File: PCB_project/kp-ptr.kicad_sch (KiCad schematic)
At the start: 41 parts, among them J1 ESP32_PROG_CON, J3 Conn_02x02_Odd_Even, U1 ESP32-S3FN8, Y1 7M40000005-40MHz

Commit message: Schematic updated
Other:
- title: KP-PTR -> KP-PTR project - PTR_mini
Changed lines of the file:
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@@
 	(paper "A4")
 	(title_block
-		(title "KP-PTR")
-		(date "2023-12-10")
-		(rev "1.1")
+		(title "KP-PTR project - PTR_mini")
+		(date "2026-09-17")
+		(rev "1.0")
 		(company "Polskie Towarzystwo Rakietowe")
 		(comment 1 "bartekM, FlyingBanana, Kretu, Red Labs, Stachu M, U.S. air force i inni")

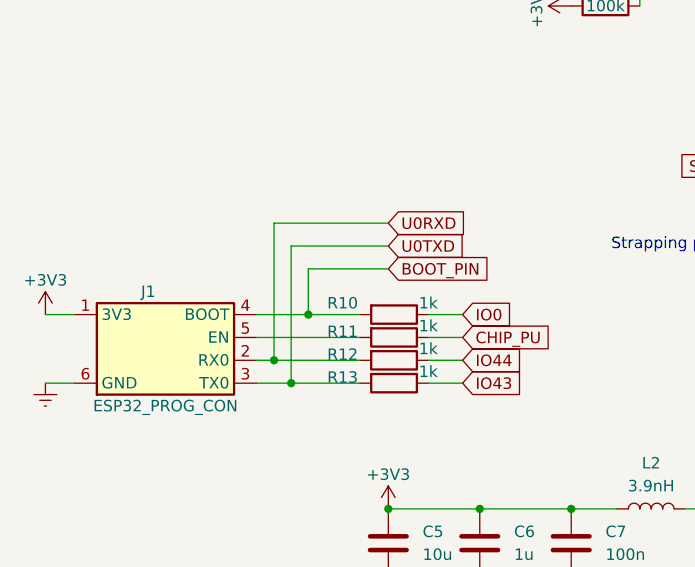
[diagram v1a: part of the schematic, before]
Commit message: Missing pullup on BOOT pin fixed. Some cleanup
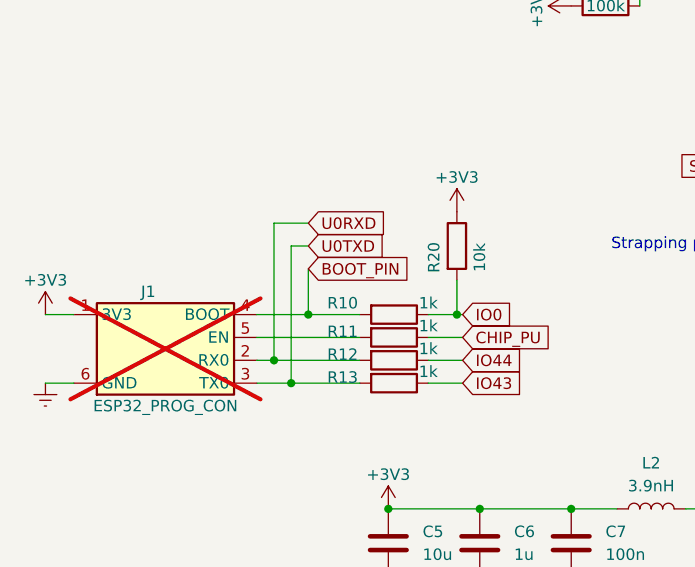
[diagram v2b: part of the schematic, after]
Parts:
- added R20: 10k, Resistor_SMD:R_0402_1005Metric, symbol Device:R
- J1: now not fitted
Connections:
- net +3V3: now also R20.1
- net IO0: now also R20.2
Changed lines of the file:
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@@
 		(color 0 0 0 0)
 	)
+	(junction
+		(at 64.77 104.14)
+		(diameter 0)
+		(color 0 0 0 0)
+	)
 	(no_connect
 		(at 171.45 64.77)
@@
 	(wire
 		(pts
+			(xy 64.77 104.14) (xy 65.405 104.14)
+		)
+		(stroke
+			(width 0)
+			(type default)
+		)
+	)
+	(wire
+		(pts
 			(xy 105.41 64.77) (xy 109.22 64.77)
 		)
@@
 	(wire
 		(pts
-			(xy 57.15 99.06) (xy 48.26 99.06)
-		)
-		(stroke
-			(width 0)
-			(type default)
-		)
-	)
-	(wire
-		(pts
 			(xy 105.41 111.76) (xy 109.22 111.76)
 		)
@@
 	(wire
 		(pts
-			(xy 61.595 104.14) (xy 65.405 104.14)
+			(xy 61.595 104.14) (xy 64.77 104.14)
 		)
 		(stroke
@@
 	(wire
 		(pts
+			(xy 64.77 100.33) (xy 64.77 104.14)
+		)
+		(stroke
+			(width 0)
+			(type default)
+		)
+	)
+	(wire
+		(pts
 			(xy 61.595 109.22) (xy 65.405 109.22)
 		)
@@
 	(wire
 		(pts
-			(xy 57.15 93.98) (xy 44.45 93.98)
+			(xy 48.26 93.98) (xy 44.45 93.98)
 		)
 		(stroke
@@
 	(wire
 		(pts
-			(xy 57.15 96.52) (xy 46.355 96.52)
+			(xy 48.26 96.52) (xy 46.355 96.52)
 		)
 		(stroke
@@
 	(global_label "U0TXD"
 		(shape input)
-		(at 57.15 96.52 0)
+		(at 48.26 96.52 0)
 		(fields_autoplaced yes)
 		(effects
@@
 		)
 		(property "Intersheetrefs" "${INTERSHEET_REFS}"
-			(at 65.5502 96.4406 0)
+			(at 56.6602 96.4406 0)
 			(hide yes)
 			(show_name no)
@@
 	(global_label "BOOT_PIN"
 		(shape input)
-		(at 57.15 99.06 0)
+		(at 48.26 99.06 0)
 		(fields_autoplaced yes)
 		(effects
@@
 		)
 		(property "Intersheetrefs" "${INTERSHEET_REFS}"
-			(at 68.6345 98.9806 0)
+			(at 59.7445 98.9806 0)
 			(hide yes)
 			(show_name no)
@@
 	(global_label "U0RXD"
 		(shape input)
-		(at 57.15 93.98 0)
+		(at 48.26 93.98 0)
 		(fields_autoplaced yes)
 		(effects
@@
 		)
 		(property "Intersheetrefs" "${INTERSHEET_REFS}"
-			(at 65.8526 93.9006 0)
+			(at 56.9626 93.9006 0)
 			(hide yes)
 			(show_name no)
@@
 	)
 	(symbol
+		(lib_id "Device:R")
+		(at 64.77 96.52 0)
+		(unit 1)
+		(body_style 1)
+		(exclude_from_sim no)
+		(in_bom yes)
+		(on_board yes)
+		(in_pos_files yes)
+		(dnp no)
+		(property "Reference" "R20"
+			(at 62.23 97.79 90)
+			(show_name no)
+			(do_not_autoplace no)
+			(effects
+				(font
+					(size 1.27 1.27)
+				)
+			)
+		)
+		(property "Value" "10k"
+			(at 67.31 97.79 90)
+			(show_name no)
+			(do_not_autoplace no)
+			(effects
+				(font
+					(size 1.27 1.27)
+				)
+			)
+		)
+		(property "Footprint" "Resistor_SMD:R_0402_1005Metric"
+			(at 62.992 96.52 90)
+			(hide yes)
+			(show_name no)
+			(do_not_autoplace no)
+			(effects
+				(font
+					(size 1.27 1.27)
+				)
+			)
+		)
+		(property "Datasheet" ""
+			(at 64.77 96.52 0)
+			(hide yes)
+			(show_name no)
+			(do_not_autoplace no)
+			(effects
+				(font
+					(size 1.27 1.27)
+				)
+			)
+		)
+		(property "Description" ""
+			(at 64.77 96.52 0)
+			(show_name no)
+			(do_not_autoplace no)
+			(effects
+				(font
+					(size 1.27 1.27)
+				)
+			)
+		)
+		(pin "1"
+		)
+		(pin "2"
+		)
+		(instances
+			(project "kp-ptr"
+				(path "/9538e4ed-27e6-4c37-b989-9859dc0d49e8"
+					(reference "R20")
+					(unit 1)
+				)
+			)
+		)
+	)
+	(symbol
 		(lib_id "Device:L")
 		(at 49.53 48.26 90)
@@
 	)
 	(symbol
+		(lib_id "power:+3.3V")
+		(at 64.77 92.71 0)
+		(unit 1)
+		(body_style 1)
+		(exclude_from_sim no)
+		(in_bom yes)
+		(on_board yes)
+		(in_pos_files yes)
+		(dnp no)
+		(property "Reference" "#PWR037"
+			(at 64.77 96.52 0)
+			(hide yes)
+			(show_name no)
+			(do_not_autoplace no)
+			(effects
+				(font
+					(size 1.27 1.27)
+				)
+			)
+		)
+		(property "Value" "+3V3"
+			(at 64.77 88.9 0)
+			(show_name no)
+			(do_not_autoplace no)
+			(effects
+				(font
+					(size 1.27 1.27)
+				)
+			)
+		)
+		(property "Footprint" ""
+			(at 64.77 92.71 0)
+			(hide yes)
+			(show_name no)
+			(do_not_autoplace no)
+			(effects
+				(font
+					(size 1.27 1.27)
+				)
+			)
+		)
+		(property "Datasheet" ""
+			(at 64.77 92.71 0)
+			(hide yes)
+			(show_name no)
+			(do_not_autoplace no)
+			(effects
+				(font
+					(size 1.27 1.27)
+				)
+			)
+		)
+		(property "Description" ""
+			(at 64.77 92.71 0)
+			(show_name no)
+			(do_not_autoplace no)
+			(effects
+				(font
+					(size 1.27 1.27)
+				)
+			)
+		)
+		(pin "1"
+		)
+		(instances
+			(project "kp-ptr"
+				(path "/9538e4ed-27e6-4c37-b989-9859dc0d49e8"
+					(reference "#PWR037")
+					(unit 1)
+				)
+			)
+		)
+	)
+	(symbol
 		(lib_id "Device:C")
 		(at 116.84 149.86 0)
@@
 		(on_board yes)
 		(in_pos_files yes)
-		(dnp no)
+		(dnp yes)
 		(property "Reference" "J1"
 			(at 30.48 101.6 0)

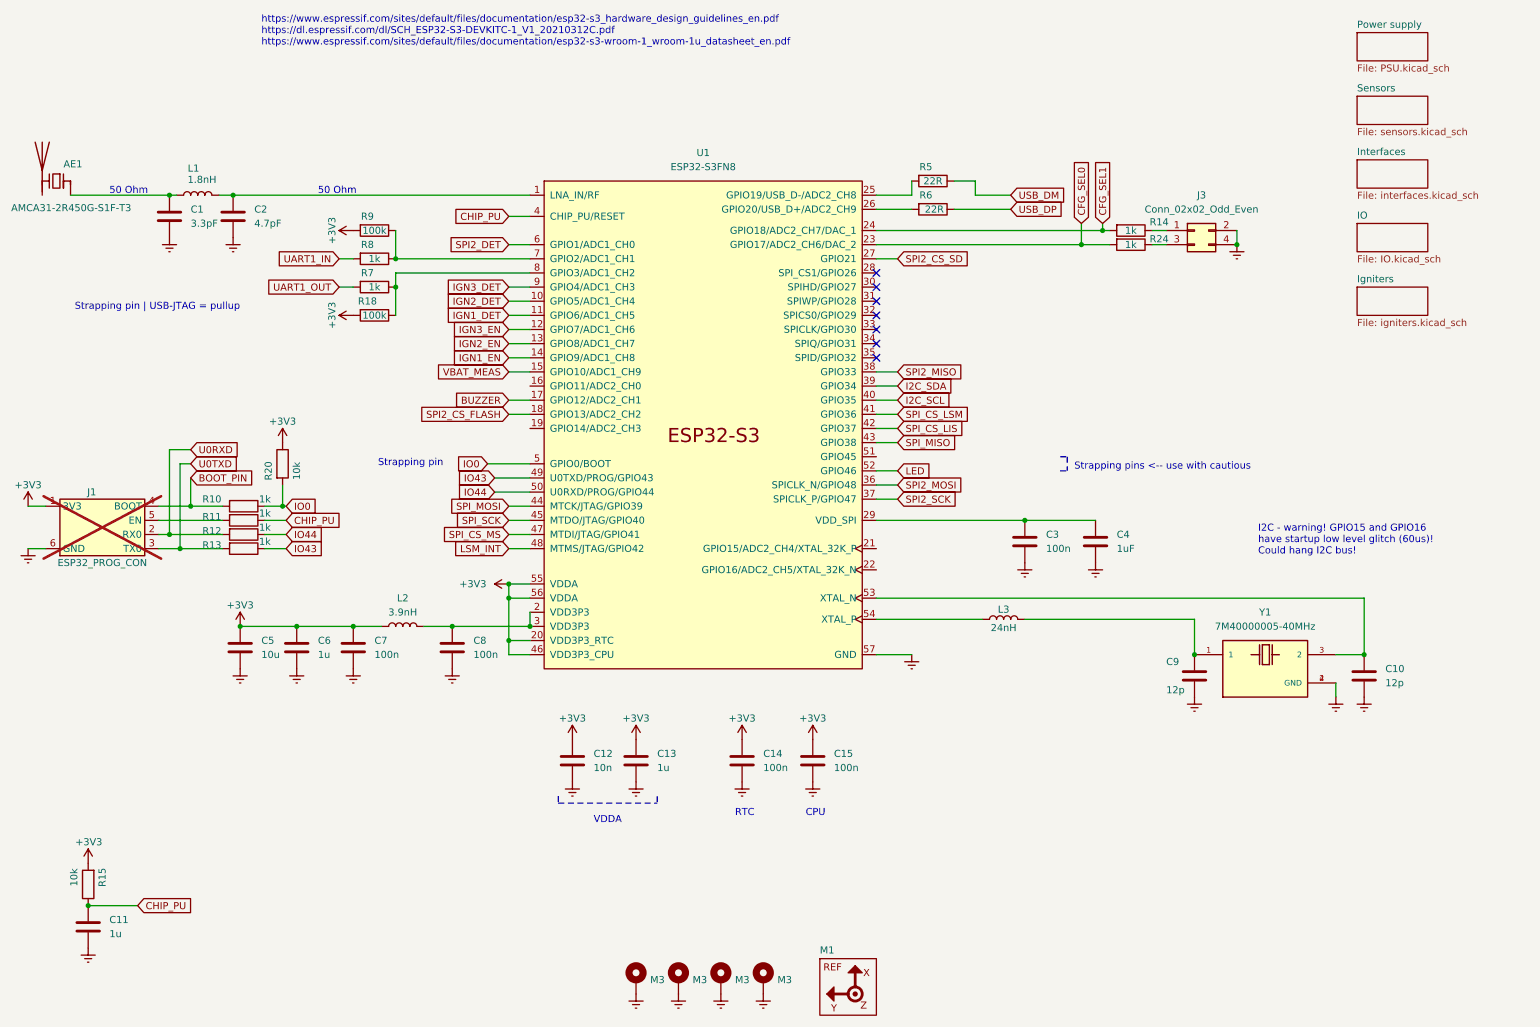
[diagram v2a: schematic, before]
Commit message: + USB connector changed to SMD
+ igniters connectors changed to single 6 pin connector
+ buzzer selected
+ crystal changed to TCXO (experimental)
+ JLC production files generated
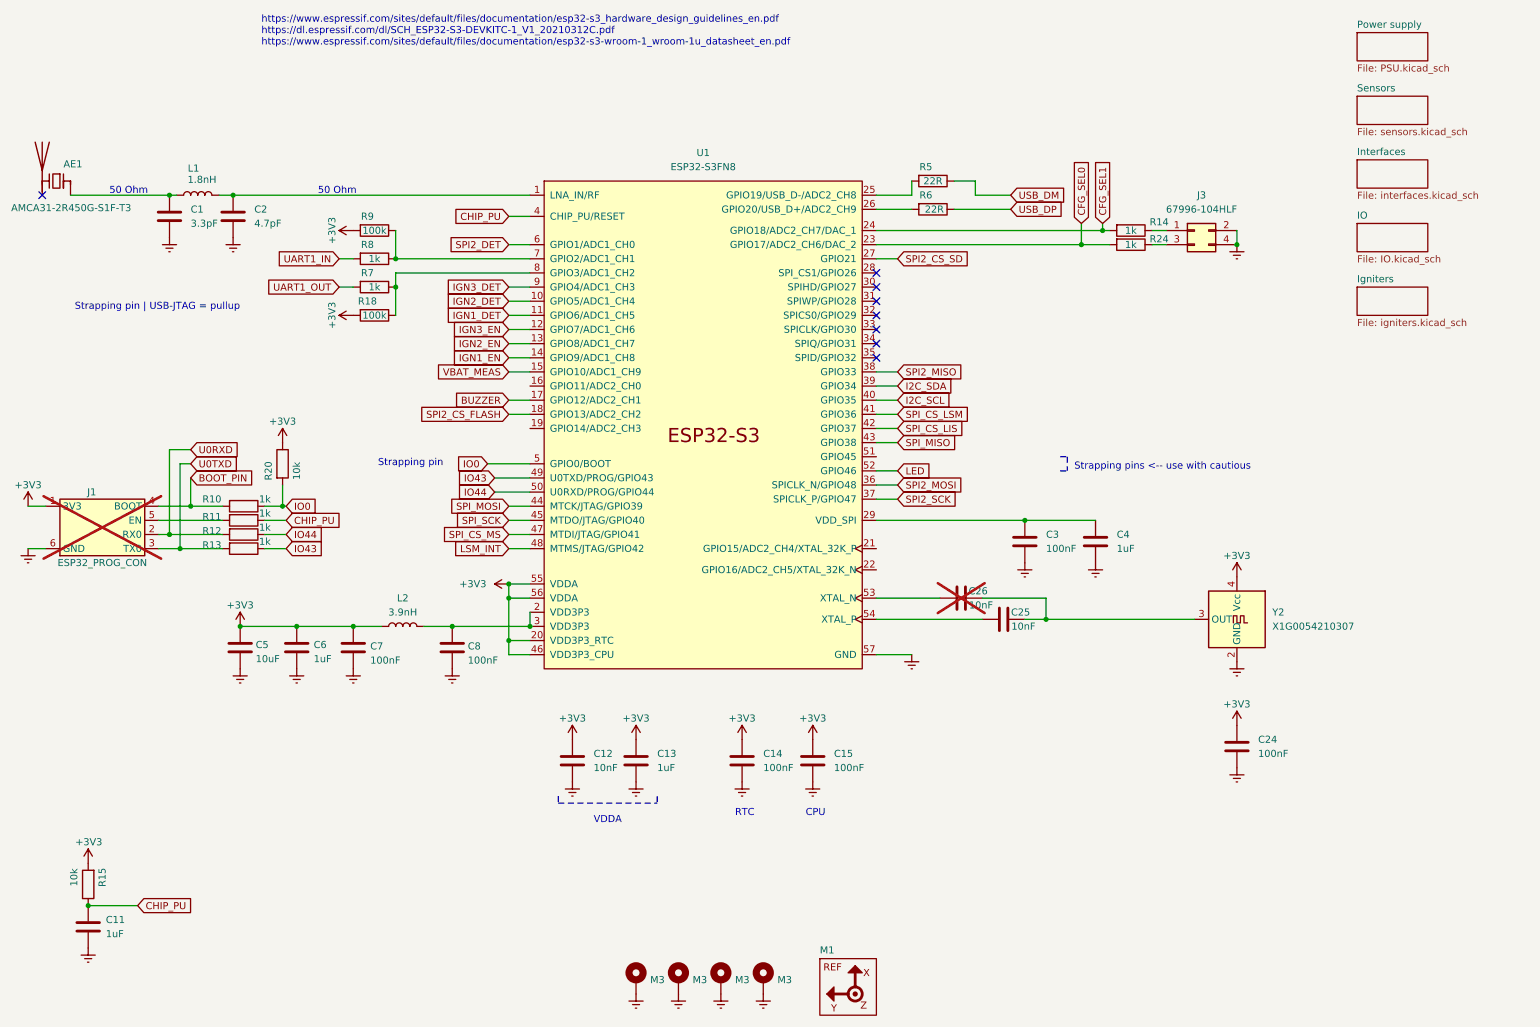
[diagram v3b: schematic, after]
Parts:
- removed C10, C9: 12p, Capacitor_SMD:C_0402_1005Metric, symbol Device:C
- removed L3: 24nH, Inductor_SMD:L_0402_1005Metric, symbol Device:L
- removed Y1: 7M40000005-40MHz, KP-PTR_lib:XTAL_TSX-3225_16.0000MF18X-AC3, symbol KP-PTR_lib:7M40000005-40MHz
- added C24: 100nF, Capacitor_SMD:C_0402_1005Metric, symbol Device:C
- added C25, C26: 10nF, Capacitor_SMD:C_0402_1005Metric, symbol Device:C
- added Y2: X1G0054210307, Oscillator:Oscillator_SMD_SeikoEpson_TG2520SMN-xxx-xxxxxx-4Pin_2.5x2.0mm, symbol Oscillator:TG2520SMN-xx.xxxxxxMhz-xxxxNM
- C11, C13, C6: value 1u -> 1uF
- C12: value 10n -> 10nF
- C14, C15, C3, C7, C8: value 100n -> 100nF
- C5: value 10u -> 10uF; footprint Capacitor_SMD:C_0402_1005Metric -> Capacitor_SMD:C_0603_1608Metric
- J1, M1: now left out of the parts list
- J3: value Conn_02x02_Odd_Even -> 67996-104HLF
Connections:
- net +3V3: now also C24.1, Y2.4 (Vcc)
- net Earth: now also C24.2, Y2.2 (GND)
- net at U1.53 (XTAL_N): now also C26.1
- net at U1.54 (XTAL_P): now also C25.1
- new net: C25.2, C26.2, Y2.3 (OUT)
- no-connect marks 7 -> 8
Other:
- note removed: "I2C - warning! GPIO15 and GPIO16 have startup low level glitch (60us)! Could hang I2C bus!"
